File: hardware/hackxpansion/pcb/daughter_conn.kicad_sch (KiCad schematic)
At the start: 1 part, among them CN3 533981471

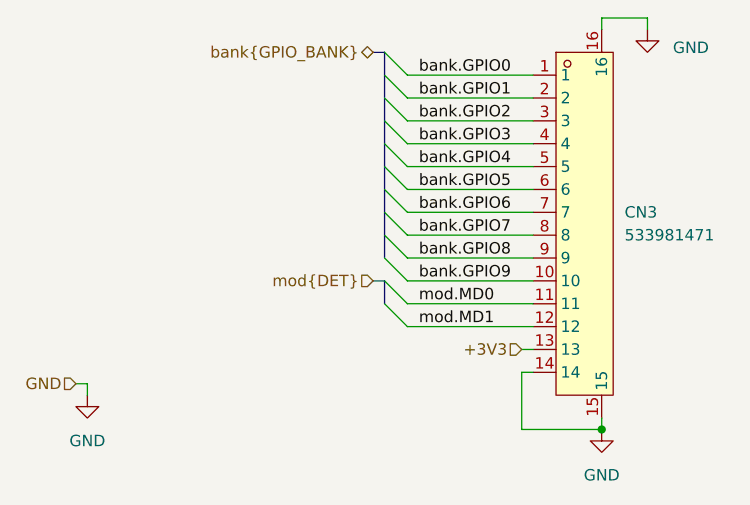
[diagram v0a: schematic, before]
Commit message: started moving resistors from daughter to main board
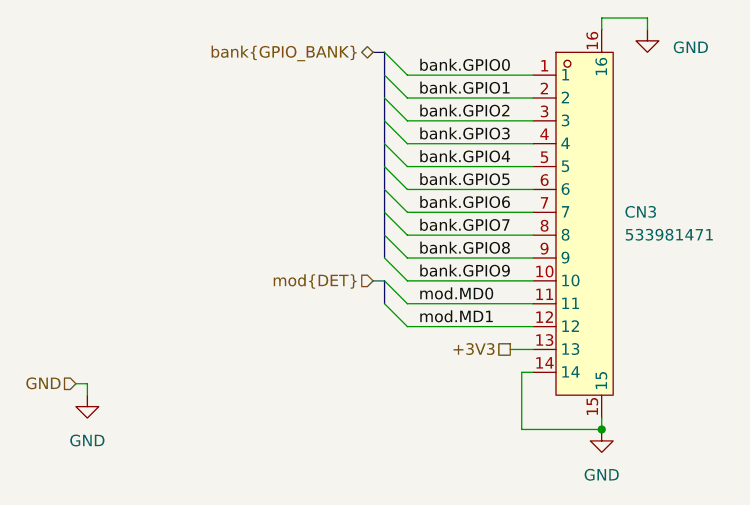
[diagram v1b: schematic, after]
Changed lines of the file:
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@@
 	(wire
 		(pts
-			(xy 152.4 82.55) (xy 153.67 82.55)
+			(xy 151.13 82.55) (xy 153.67 82.55)
 		)
 		(stroke
@@
 	)
 	(hierarchical_label "+3V3"
-		(shape input)
-		(at 152.4 82.55 180)
-		(effects
-			(font
+		(shape passive)
+		(at 151.13 82.55 180)
+		(effects
+			(font
